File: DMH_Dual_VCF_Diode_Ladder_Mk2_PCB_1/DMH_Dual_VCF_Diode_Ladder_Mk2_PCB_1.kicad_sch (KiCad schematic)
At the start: 0 parts

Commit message: Added CV3 and Drive CV to I/O pages
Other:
- sheet CV Processing ports: added CV3 A Input, CV3 B Input, Link CV Switch; removed Bus CV A Input, Bus CV B Input, Link Switch
- sheet Inputs and Outputs A ports: added CV 3 Jack, CV 3 TN, Drive CV Jack; removed Feed Switch
- sheet Inputs and Outputs B ports: added CV 3 Jack, CV3 TN, Drive CV Jack, Drive CV TN; removed none

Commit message: Added board-to-board pins to schematic
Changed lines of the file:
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@@
+	(wire
+		(pts
+			(xy 73.66 118.11) (xy 73.66 129.54)
+		)
+		(stroke
+			(width 0)
+			(type default)
+		)
+	)
 	(wire
 		(pts
@@
 	(wire
 		(pts
+			(xy 73.66 129.54) (xy 76.2 129.54)
+		)
+		(stroke
+			(width 0)
+			(type default)
+		)
+	)
+	(wire
+		(pts
 			(xy 101.6 22.86) (xy 123.19 22.86)
 		)
@@
 		)
 		(stroke
+			(width 0)
+			(type default)
+		)
+	)
+	(wire
+		(pts
+			(xy 76.2 118.11) (xy 73.66 118.11)
+		)
+		(stroke

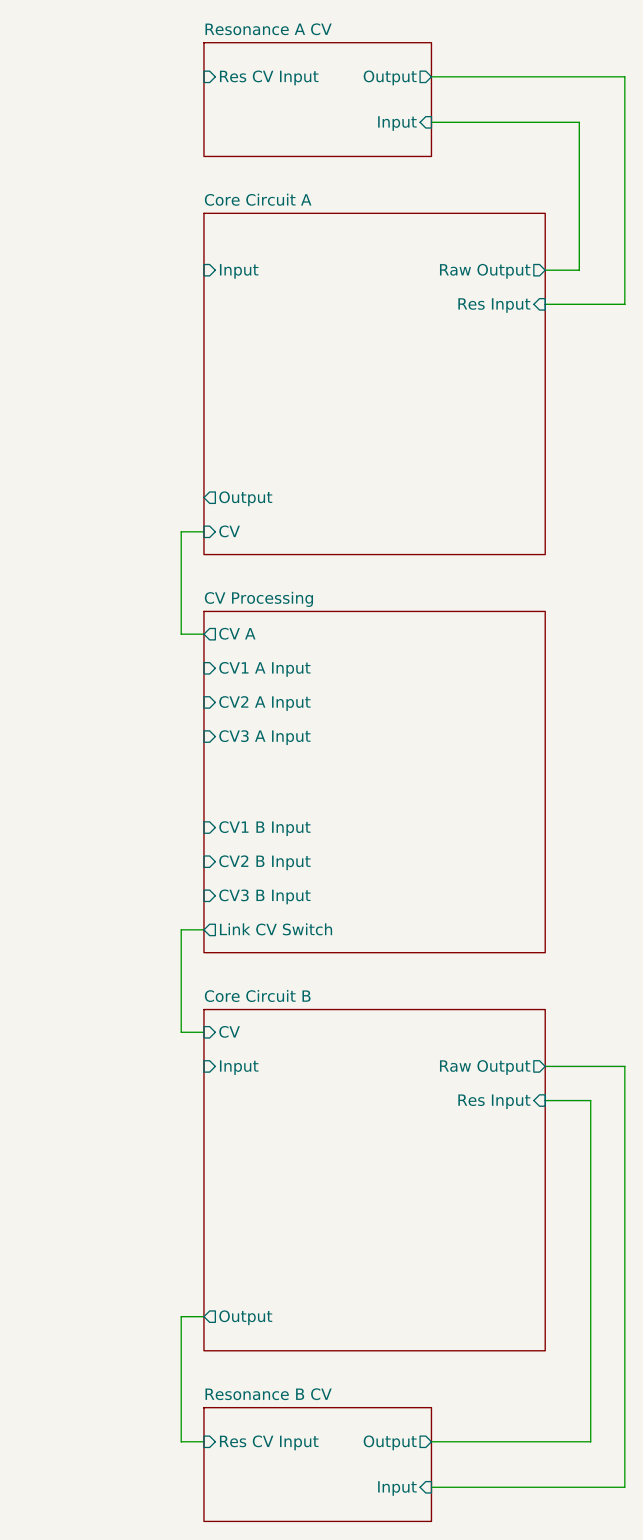
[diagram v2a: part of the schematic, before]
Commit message: Created Drive CV circuits
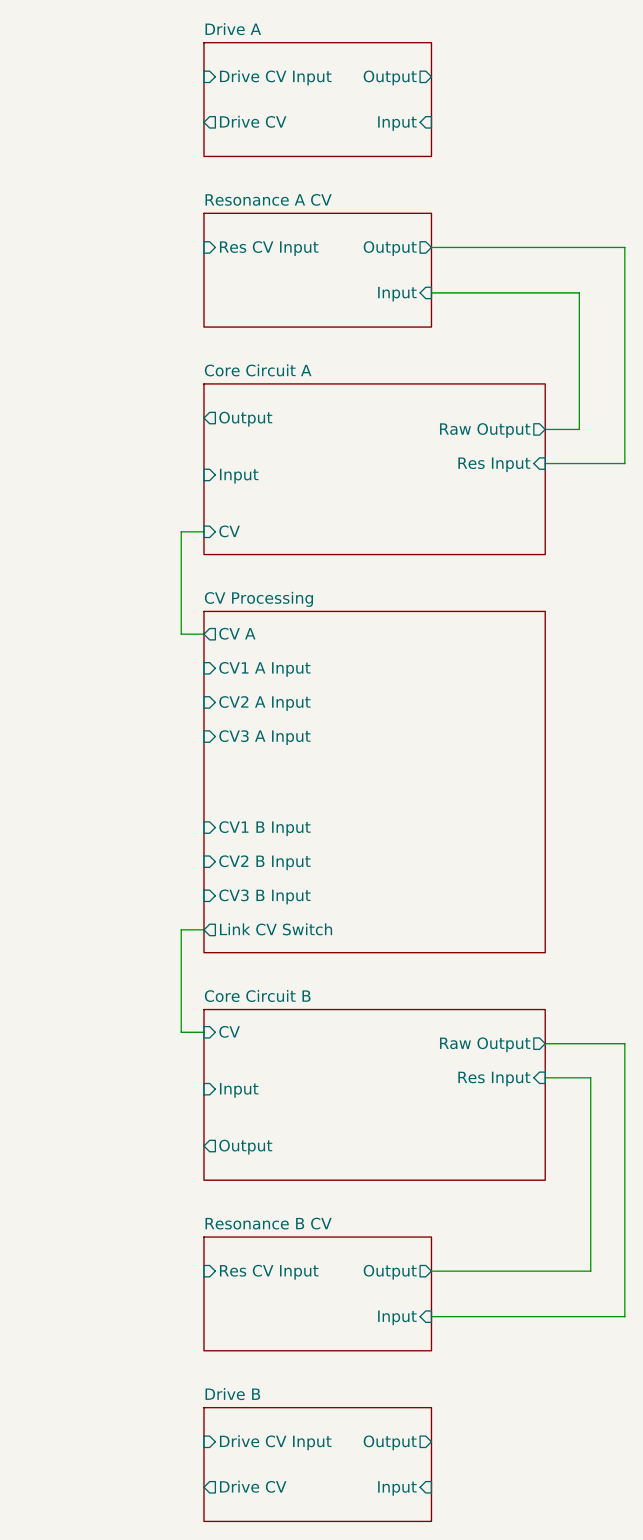
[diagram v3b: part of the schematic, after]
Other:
- added sheet Drive A (Drive_A.kicad_sch)
- added sheet Drive B (Drive_B.kicad_sch)

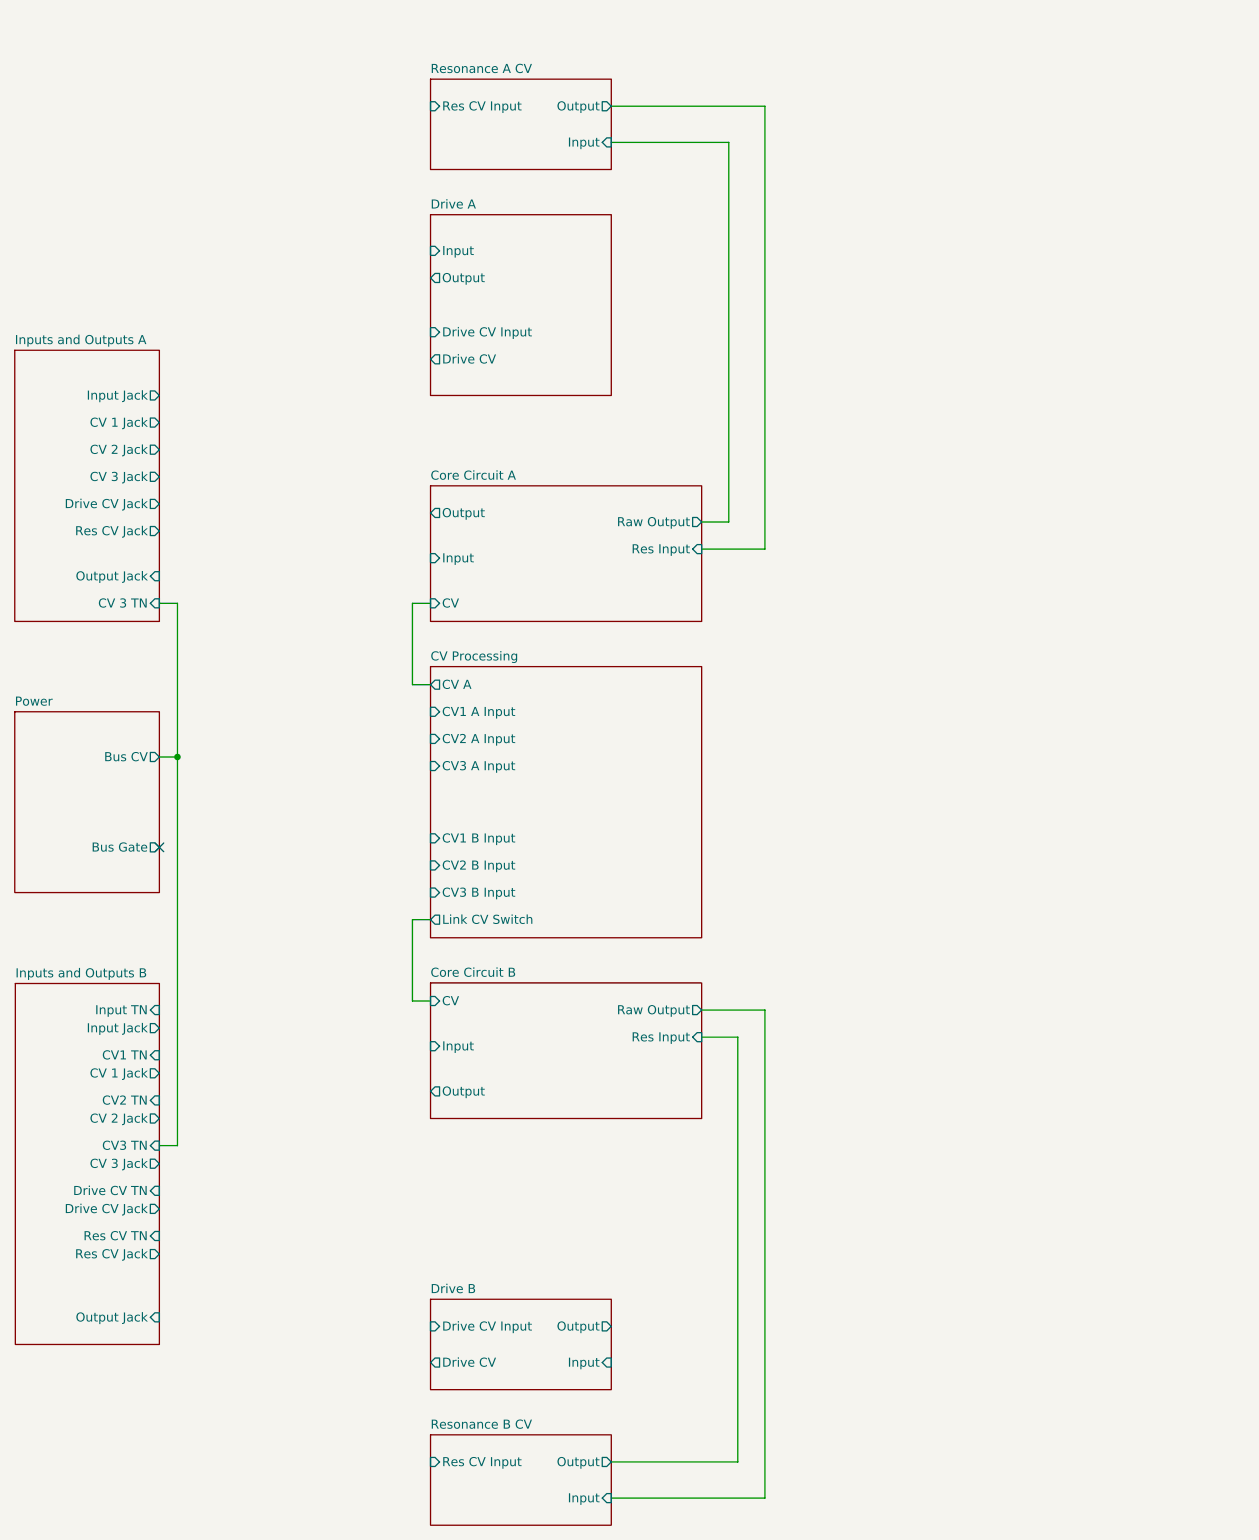
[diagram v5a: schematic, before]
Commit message: Connected all hierarchical pins
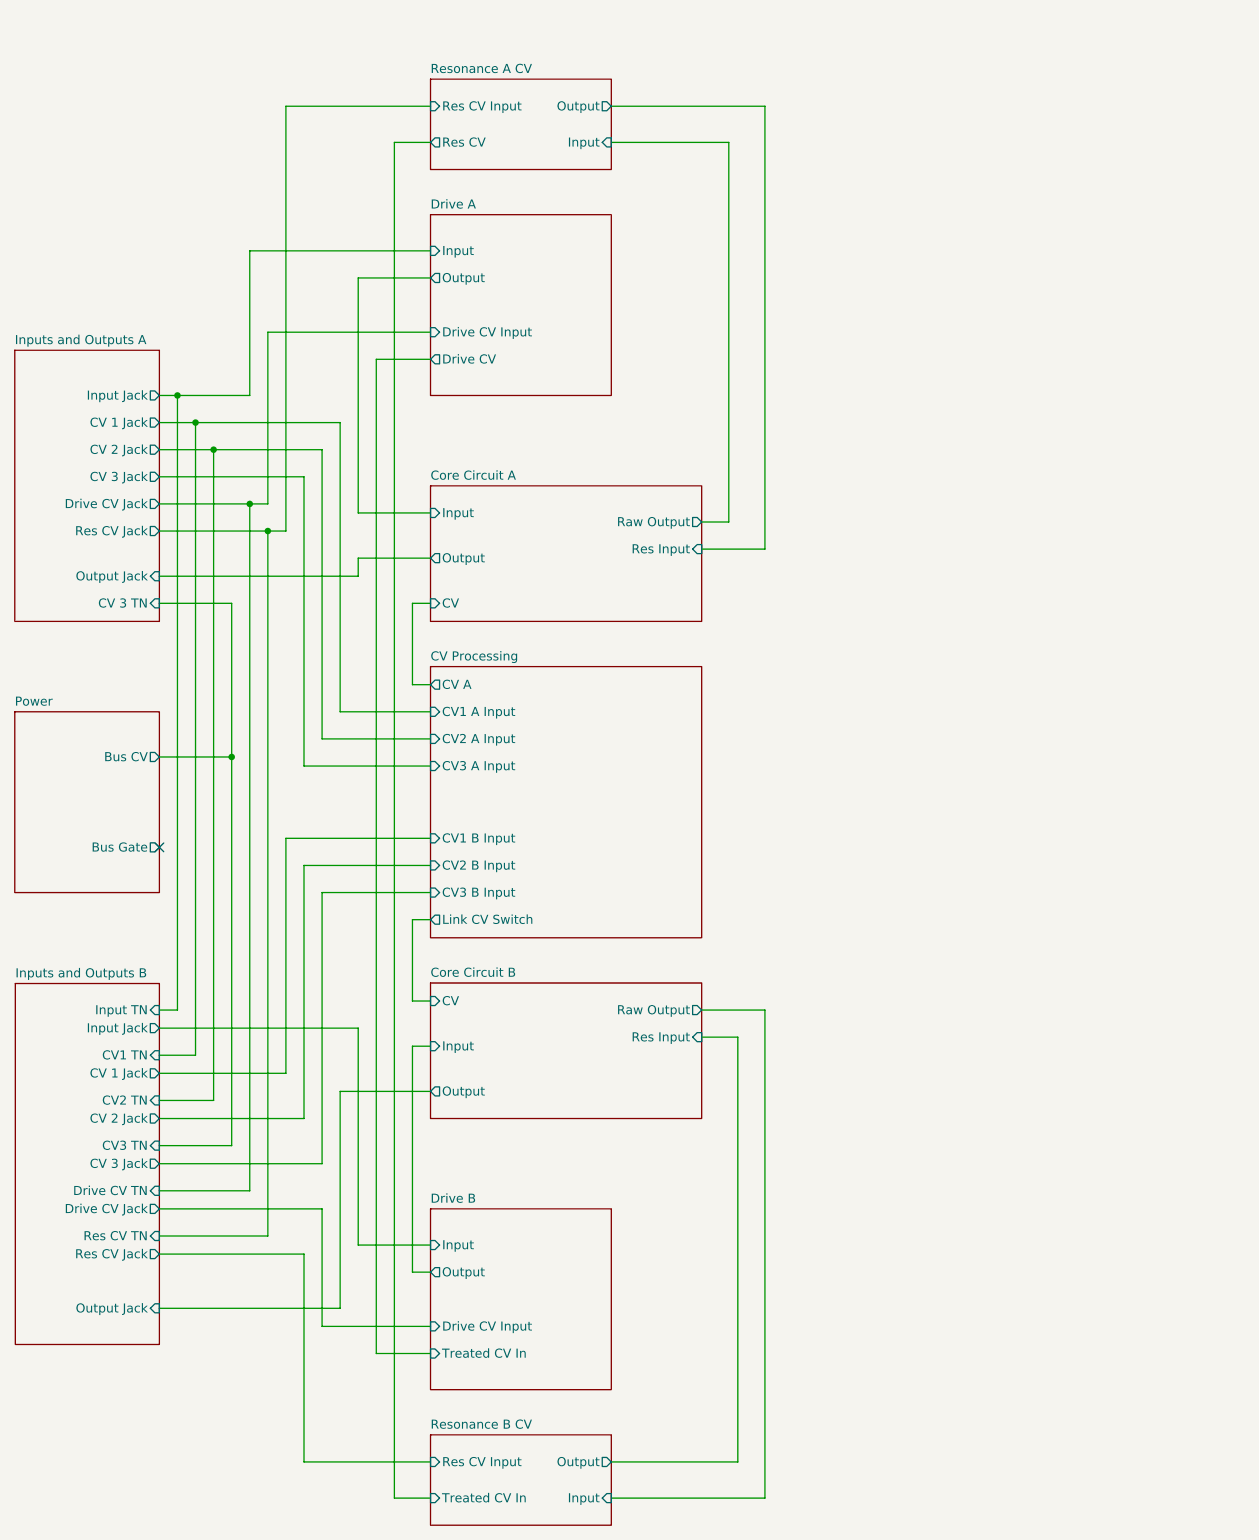
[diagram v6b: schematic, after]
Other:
- sheet Drive B ports: added Treated CV In; removed Drive CV
- sheet Resonance A CV ports: added Res CV; removed none
- sheet Resonance B CV ports: added Treated CV In; removed none

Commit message: Reannotated OpAmps and cleared errors
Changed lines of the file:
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@@
 	(wire
 		(pts
-			(xy 53.34 85.09) (xy 53.34 60.96)
+			(xy 50.8 85.09) (xy 50.8 60.96)
 		)
 		(stroke
@@
 	(wire
 		(pts
-			(xy 50.8 49.53) (xy 76.2 49.53)
+			(xy 48.26 49.53) (xy 76.2 49.53)
 		)
 		(stroke
@@
 	(wire
 		(pts
-			(xy 55.88 29.21) (xy 76.2 29.21)
+			(xy 53.34 29.21) (xy 76.2 29.21)
 		)
 		(stroke
@@
 	(wire
 		(pts
-			(xy 50.8 85.09) (xy 53.34 85.09)
-		)
-		(stroke
-			(width 0)
-			(type default)
-		)
-	)
-	(wire
-		(pts
-			(xy 55.88 88.9) (xy 55.88 29.21)
+			(xy 53.34 88.9) (xy 53.34 29.21)
 		)
 		(stroke
@@
 	(wire
 		(pts
-			(xy 40.64 69.85) (xy 50.8 69.85)
+			(xy 40.64 69.85) (xy 48.26 69.85)
 		)
 		(stroke
@@
 	(wire
 		(pts
-			(xy 53.34 88.9) (xy 55.88 88.9)
-		)
-		(stroke
-			(width 0)
-			(type default)
-		)
-	)
-	(wire
-		(pts
 			(xy 60.96 118.11) (xy 76.2 118.11)
 		)
@@
 	(wire
 		(pts
-			(xy 53.34 60.96) (xy 76.2 60.96)
+			(xy 50.8 60.96) (xy 76.2 60.96)
 		)
 		(stroke
@@
 	(wire
 		(pts
-			(xy 50.8 69.85) (xy 50.8 49.53)
-		)
-		(stroke
+			(xy 48.26 69.85) (xy 48.26 49.53)
+		)
+		(stroke
